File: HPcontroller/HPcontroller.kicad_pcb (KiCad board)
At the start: 4 copper layers, 78 x 57 mm, 65 parts, among them J1 54-00174, J2 USB_C_Receptacle, J3 Conn_01x04_Pin, J4 Conn_01x01_Pin, J5 54-00174, J6 Conn_01x01_Pin, Q2 AON7410, Q3 Q_Dual_NMOS_S1G1S2G2D2D2D1D1, U1 MCP23017_SO, U10 SN74LVC1G14DBV, U11 SN74LVC1G14DBV, U2 MCP3021A1T-E/OT, U3 HEF4043BT, U4 NCP81071B, U6 SN74LV4052ADR, U7 Adafruit_QTPY_ESP32-C3, U8 IP2721, U9 SN74AHC1G08DBVR

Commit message: v3 routing
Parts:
- removed C5, C9: 1uF, Capacitor_SMD:C_0805_2012Metric_Pad1.18x1.45mm_HandSolder
- removed D2: ESDA6V1BC6, Package_TO_SOT_SMD:SOT-23-6
- removed D_HEAT1, D_HOT1, D_POW1, D_RUN1: LED, LED_SMD:LED_0603_1608Metric_Pad1.05x0.95mm_HandSolder
- removed H2: MountingHole, MountingHole:MountingHole_2.7mm_M2.5
- removed J1: 54-00174, HPfootprint:TENSILITY_54-00174
- removed J3: Conn_01x04_Pin, Connector_PinHeader_2.54mm:PinHeader_1x04_P2.54mm_Vertical
- removed J4, J6: Conn_01x01_Pin, HPfootprint:S7051-42R
- removed MOD1: K7803JT-500R3-LB, HPfootprint:MORNSUN_K7803JT-500R3-LB
- removed Q3: Q_Dual_NMOS_S1G1S2G2D2D2D1D1, Package_SO:SOIC-8_3.9x4.9mm_P1.27mm
- removed RTHERM: 10kTHERM, Resistor_SMD:R_0805_2012Metric_Pad1.20x1.40mm_HandSolder
- removed SWDEC2, SWINC3, SWINC4, SWRUN2: SW_SPST, Button_Switch_SMD:SW_SPST_PTS645
- removed U1: MCP23017_SO, Package_SO:SOIC-28W_7.5x17.9mm_P1.27mm
- added C15: 10uF 50V, Capacitor_SMD:C_1206_3216Metric_Pad1.33x1.80mm_HandSolder, F.Cu at (164.6, 138.5)
- added D1: LED, LED_SMD:LED_0603_1608Metric_Pad1.05x0.95mm_HandSolder, F.Cu at (173.4, 137.8)
- added H4: MountingHole, MountingHole:MountingHole_2.7mm_M2.5, F.Cu at (107.8, 122.8)
- added Q1: ~, hotplate_Library:LFPAK56D, F.Cu at (181.0, 134.5)
- added R11: 100, Resistor_SMD:R_0402_1005Metric_Pad0.72x0.64mm_HandSolder, F.Cu at (168.4, 138.0)
- added R14: 10, Resistor_SMD:R_0402_1005Metric_Pad0.72x0.64mm_HandSolder, F.Cu at (172.9, 135.0)
- added R15: 10, Resistor_SMD:R_0402_1005Metric_Pad0.72x0.64mm_HandSolder, F.Cu at (172.9, 136.2)
- added R16: 5k1 1%, Resistor_SMD:R_0402_1005Metric_Pad0.72x0.64mm_HandSolder, F.Cu at (176.0, 126.9)
- added R17: 5k1 1%, Resistor_SMD:R_0402_1005Metric_Pad0.72x0.64mm_HandSolder, F.Cu at (176.0, 129.3)
- added R6: 26k, Resistor_SMD:R_0603_1608Metric_Pad0.98x0.95mm_HandSolder, F.Cu at (175.6, 131.5)
- added RTHERM1: 100kTherm, Resistor_SMD:R_0805_2012Metric_Pad1.20x1.40mm_HandSolder, F.Cu at (135.3, 147.0)
- added TP1: TestPoint, TestPoint:TestPoint_Pad_D1.5mm, F.Cu at (163.2, 127.7)
- added TP2: TestPoint, TestPoint:TestPoint_Pad_D1.5mm, F.Cu at (158.2, 126.5)
- added TP8: TestPoint, TestPoint:TestPoint_Pad_D1.5mm, F.Cu at (171.0, 140.0)
- added TP_3V1: TestPoint, TestPoint:TestPoint_Pad_D1.0mm, F.Cu at (152.8, 143.6)
- added U5: AP33771C, Package_DFN_QFN:DFN-14-1EP_3x3mm_P0.4mm_EP1.78x2.35mm, F.Cu at (172.8, 131.1)
- C14: value 10uF -> 1uF 25V; footprint Capacitor_SMD:C_0805_2012Metric -> Capacitor_SMD:C_0402_1005Metric_Pad0.74x0.62mm_HandSolder
- C6: value 1uF -> 10uF 50V; footprint Capacitor_SMD:C_0603_1608Metric -> Capacitor_SMD:C_1206_3216Metric_Pad1.33x1.80mm_HandSolder
- J2: value USB_C_Receptacle -> UJ20-C-H-G-SMT-1-P16-TR; footprint Connector_USB:USB_C_Receptacle_JAE_DX07S016JA1R1500 -> hotplate_Library:SAMESKY_UJ20-C-H-G-SMT-1-P16-TR
- J5: footprint HPfootprint:TENSILITY_54-00174 -> hotplate_Library:TENSILITY_54-00174
- Q2: value AON7410 -> ~; footprint HPfootprint:DFN3X3A_8L_EPA1_P_AOS -> hotplate_Library:LFPAK56D
- R1: value 5.1k -> 5k1 1%; footprint Resistor_SMD:R_0603_1608Metric -> Resistor_SMD:R_0402_1005Metric_Pad0.72x0.64mm_HandSolder
- R10: value RTHERM -> 100kTherm
- R21: moved to F.Cu
- R4: value 5.1k -> 1k; footprint Resistor_SMD:R_0603_1608Metric -> Resistor_SMD:R_0402_1005Metric_Pad0.72x0.64mm_HandSolder
- R5: value 100k -> 5m; footprint Resistor_SMD:R_0603_1608Metric -> Resistor_SMD:R_0603_1608Metric_Pad0.98x0.95mm_HandSolder
- U3: footprint HPfootprint:SOT109-1_NXP -> Package_SO:SO-16_3.9x9.9mm_P1.27mm
- U7: footprint HPfootprint:QTPY ESP32 C3 -> hotplate_Library:XIAO-ESP32C3-SMD-cutout
- U8: value IP2721 -> ~; footprint Package_SO:TSSOP-16_4.4x5mm_P0.65mm -> hotplate_Library:D78B33-0.5
- moved R21 75.1 mm to (107.9, 139.0)
- moved R22 71.9 mm to (123.4, 143.2), turned to 90 degrees
- moved R24 68.5 mm to (100.8, 133.8), turned to 180 degrees
- moved R13 61.2 mm to (88.5, 128.5), turned to 180 degrees
- moved D_RTD1 61.1 mm to (88.5, 130.5), turned to 180 degrees
- moved C10 59.2 mm to (100.2, 144.7)
- moved SWRST2 57.3 mm to (114.5, 123.7), turned to 90 degrees
- moved R12 55.3 mm to (135.3, 144.7), turned to 180 degrees
- moved C3 55.0 mm to (179.4, 145.7), turned to 0 degrees
- moved U9 54.5 mm to (92.2, 144.8), turned to 180 degrees
- moved R7 53.6 mm to (145.0, 139.2)
- moved R8 53.5 mm to (147.2, 139.2)
- moved H3 53.1 mm to (162.2, 122.8)
- moved R4 52.9 mm to (174.7, 135.5), turned to -90 degrees
- moved C7 52.8 mm to (160.6, 138.0), turned to 90 degrees
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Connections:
- C14 pad 1: +20V_USBPD -> Net-(U5-V5V)
- C2 pad 1: +20V_USBPD -> +28V
- C3 pad 1: +20V_USBPD -> +28V
- C6 pad 1: VBUS -> /USB POWER IN/VUSB_RAW
- C7 pad 1: +20V_USBPD -> +28V
- D3 pad 1: +20V_USBPD -> +28V
- J2 pad A6: unconnected-(J2-D+-PadA6) -> /USB POWER IN/DP
- J2 pad A7: unconnected-(J2-D--PadA7) -> /USB POWER IN/DN
- J2 pad B6: unconnected-(J2-D+-PadB6) -> /USB POWER IN/DP
- J2 pad B7: unconnected-(J2-D--PadB7) -> /USB POWER IN/DN
- Q2 pad 1: +20V_USBPD -> Net-(Q2-S1)
- Q2 pad 2: +20V_USBPD -> Net-(Q2-G1)
- Q2 pad 3: +20V_USBPD -> Net-(Q2-S1)
- Q2 pad 4: Net-(Q2-G) -> Net-(Q2-G2)
- Q2 pad 5: VBUS -> Net-(Q2-D2)
- Q2 pad 7: VBUS -> +28V
- R1 pad 1: /USB POWER IN/CC1 -> /USB POWER IN/CC2
- R4 pad 1: /USB POWER IN/CC2 -> Net-(U5-LED)
- R4 pad 2: GND -> Net-(D1-A)
- R5 pad 1: VBUS -> /USB POWER IN/VUSB_RAW
- R5 pad 2: Net-(U8-SEL) -> Net-(Q2-D2)
- U4 pad 6: +20V_USBPD -> +28V
- U7 pad 10: /INTA -> unconnected-(U7-MISO-Pad10)
- U8 pad 1: Net-(Q2-G) -> +28V
- U8 pad 2: VBUS -> GND
- U8 pad 3: (no net) -> +3V3
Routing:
- net /INTA: track 91.0 -> 0.00 mm, vias 2 -> 0
- net /SDA: track 139.2 -> 60.2 mm
- net GND: track 122.5 -> 53.2 mm, vias 43 -> 32
- net Net-(U4-ENA): track 39.6 -> 101.2 mm, vias 2 -> 0
- net /SCL: track 128.0 -> 68.0 mm, vias 3 -> 2
- net +20V_USBPD: track 55.2 -> 0.00 mm, vias 2 -> 0
- net +28V: track 0.00 -> 48.3 mm
- net /HEATER DRIVE/ENABLE_HEATER_DRIVE: track 74.8 -> 26.7 mm
- net Net-(U3-1S): track 42.2 -> 2.25 mm
- net /Controlpad/RUN_LED: track 29.3 -> 0.00 mm
- net Net-(U2-Ain): track 41.5 -> 12.9 mm
- net /Controlpad/HOT: track 28.4 -> 0.00 mm
- net /Controlpad/POW: track 28.1 -> 0.00 mm
- net /USB POWER IN/VUSB_RAW: track 0.00 -> 26.7 mm, vias 0 -> 2
- net /Controlpad/RUN: track 23.8 -> 0.00 mm
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- added copper zone on F.Cu, net +28V
- added copper zone on In1.Cu, net +3V3
- added copper zone on In2.Cu, net GND
- removed copper zone on F.Cu, net +20V_USBPD
- removed copper zone on In2.Cu, net +3V3
- removed copper zone on In1.Cu, net GND
- removed copper zone on F.Cu, net Net-(D3-A)
- removed copper zone on F.Cu, net VBUS
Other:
- board size 78 x 57 mm -> 100 x 30 mm
- board text removed: "HP_POWER"

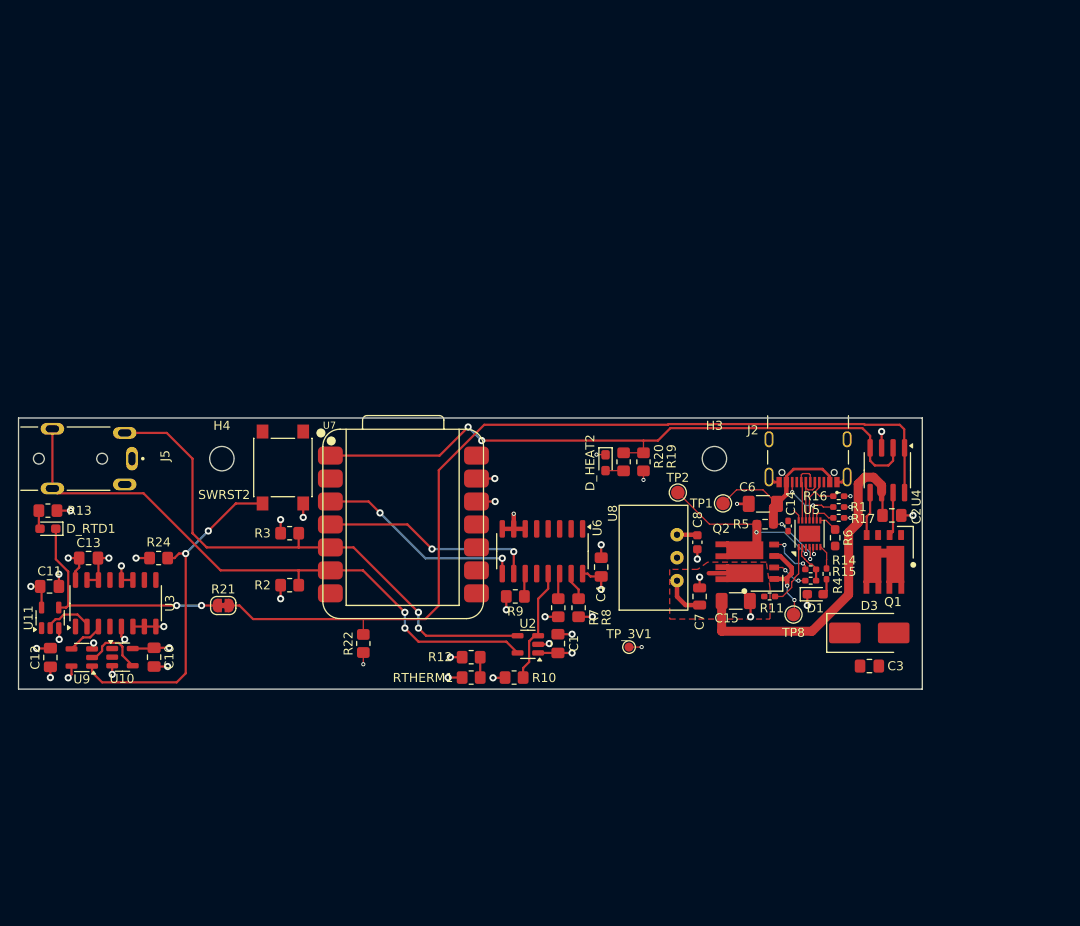
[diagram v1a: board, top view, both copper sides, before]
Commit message: new temp circuit
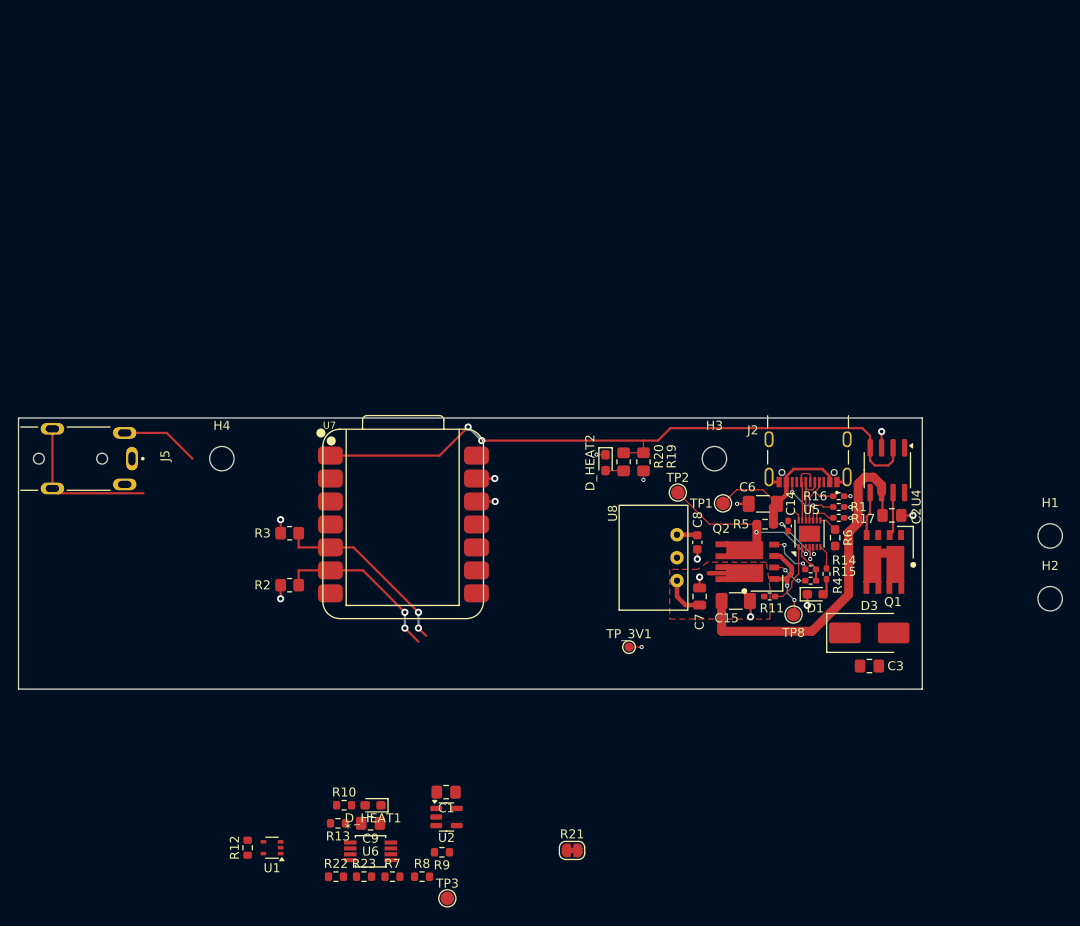
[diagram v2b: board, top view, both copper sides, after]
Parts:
- removed C10, C11, C12, C13, C4: 1uF, Capacitor_SMD:C_0805_2012Metric_Pad1.18x1.45mm_HandSolder
- removed D_RTD1: LED, LED_SMD:LED_0603_1608Metric_Pad1.05x0.95mm_HandSolder
- removed R24: 10k, Resistor_SMD:R_0805_2012Metric_Pad1.20x1.40mm_HandSolder
- removed RTHERM1: 100kTherm, Resistor_SMD:R_0805_2012Metric_Pad1.20x1.40mm_HandSolder
- removed SWRST2: SW_SPST, Button_Switch_SMD:SW_SPST_PTS645
- removed U10, U11: SN74LVC1G14DBV, Package_TO_SOT_SMD:SOT-23-5
- removed U3: HEF4043BT, Package_SO:SO-16_3.9x9.9mm_P1.27mm
- removed U9: SN74AHC1G08DBVR, Package_TO_SOT_SMD:SOT-23-5
- added C9: 1uF, Capacitor_SMD:C_0805_2012Metric_Pad1.18x1.45mm_HandSolder, F.Cu at (124.2, 163.1)
- added D_HEAT1: LED, LED_SMD:LED_0603_1608Metric_Pad1.05x0.95mm_HandSolder, F.Cu at (124.5, 161.1)
- added H1: MountingHole, MountingHole:MountingHole_2.7mm_M2.5, F.Cu at (199.4, 131.3)
- added H2: MountingHole, MountingHole:MountingHole_2.7mm_M2.5, F.Cu at (199.4, 138.2)
- added R23: 952, Resistor_SMD:R_0603_1608Metric, F.Cu at (123.5, 169.0)
- added TP3: TestPoint, TestPoint:TestPoint_Pad_D1.5mm, F.Cu at (132.7, 171.4)
- added U1: PSSI2021SAY, Package_TO_SOT_SMD:SOT-353_SC-70-5, F.Cu at (113.3, 165.8)
- R10: value 100kTherm -> 100; footprint Resistor_SMD:R_0805_2012Metric_Pad1.20x1.40mm_HandSolder -> Resistor_SMD:R_0603_1608Metric
- R12: value 420 -> 626; footprint Resistor_SMD:R_0805_2012Metric_Pad1.20x1.40mm_HandSolder -> Resistor_SMD:R_0603_1608Metric
- R13: value 100 -> 2k; footprint Resistor_SMD:R_0805_2012Metric_Pad1.20x1.40mm_HandSolder -> Resistor_SMD:R_0603_1608Metric
- R22: value 10k -> 1666; footprint Resistor_SMD:R_0805_2012Metric_Pad1.20x1.40mm_HandSolder -> Resistor_SMD:R_0603_1608Metric
- R7: value 100k -> 111; footprint Resistor_SMD:R_0805_2012Metric_Pad1.20x1.40mm_HandSolder -> Resistor_SMD:R_0603_1608Metric
- R8: value 10k -> 1000; footprint Resistor_SMD:R_0805_2012Metric_Pad1.20x1.40mm_HandSolder -> Resistor_SMD:R_0603_1608Metric
- R9: value 1k -> 0; footprint Resistor_SMD:R_0805_2012Metric_Pad1.20x1.40mm_HandSolder -> Resistor_SMD:R_0603_1608Metric
- U6: value SN74LV4052ADR -> LM2904; footprint Package_SO:SOIC-16_3.9x9.9mm_P1.27mm -> hotplate_Library:MINISO8_3P1X3P2X0P65_STM
- moved R13 47.2 mm to (120.6, 163.1)
- moved R21 47.2 mm to (146.5, 166.1)
- moved U6 38.3 mm to (124.2, 166.2), turned to 0 degrees
- moved R7 35.0 mm to (126.6, 169.0), turned to 0 degrees
- moved R8 34.4 mm to (129.9, 169.0), turned to 0 degrees
- moved R12 32.5 mm to (110.6, 165.8), turned to 90 degrees
- moved R9 29.4 mm to (132.1, 166.3)
- moved R22 26.0 mm to (120.4, 169.0), turned to 0 degrees
- moved R10 23.5 mm to (121.3, 161.1)
- moved U2 21.1 mm to (132.6, 162.4), turned to 0 degrees
- moved C1 20.6 mm to (132.6, 159.7), turned to 0 degrees
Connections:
- R10 pad 2: Net-(U2-Ain) -> Net-(D_HEAT1-A)
- R12 pad 1: Net-(U3-1S) -> +3V3
- R12 pad 2: GND -> Net-(R12-Pad2)
- R13 pad 1: +3V3 -> Net-(U2-Ain)
- R13 pad 2: Net-(D_RTD1-A) -> Net-(U6A--)
- R22 pad 2: Net-(U4-ENA) -> Net-(U6A--)
- R7 pad 1: Net-(U6-1Y1) -> Net-(U6B-+)
- R7 pad 2: GND -> Net-(D4-A)
- R8 pad 1: Net-(U6-1Y2) -> Net-(D4-A)
- R9 pad 1: Net-(U6-1Y3) -> Net-(D4-K)
- R9 pad 2: GND -> Net-(R9-Pad2)
- U6 pad 1: unconnected-(U6-2Y0-Pad1) -> Net-(U2-Ain)
- U6 pad 2: unconnected-(U6-2Y2-Pad2) -> Net-(U6A--)
- U6 pad 3: unconnected-(U6-2-COM-Pad3) -> Net-(U6A-+)
- U6 pad 4: unconnected-(U6-2Y3-Pad4) -> GND
- U6 pad 5: unconnected-(U6-2Y1-Pad5) -> Net-(U6B-+)
- U6 pad 6: GND -> Net-(U2-Ain)
- U6 pad 7: GND -> /HEATER DRIVE/ENABLE_HEATER_DRIVE
- U6 pad 8: GND -> +3V3
- U7 pad 3: /SEL_B -> unconnected-(U7-A2-Pad3)
- U7 pad 4: /SEL_A -> unconnected-(U7-A3-Pad4)
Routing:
- net Net-(U4-ENA): track 101.2 -> 0.00 mm
- net Net-(SWRST2-A): track 38.4 -> 0.00 mm, vias 2 -> 0
- net GND: track 53.2 -> 18.7 mm, vias 32 -> 14
- net /SCL: track 68.0 -> 35.8 mm
- net /SDA: track 60.2 -> 29.4 mm
- net +3V3: track 38.9 -> 8.74 mm, vias 17 -> 4
- net /HEATER DRIVE/ENABLE_HEATER_DRIVE: track 26.7 -> 0.00 mm, vias 2 -> 0
- net /SEL_A: track 24.0 -> 0.00 mm, vias 2 -> 0
- net /SEL_B: track 23.3 -> 0.00 mm, vias 2 -> 0
- net Net-(U2-Ain): track 12.9 -> 0.00 mm
- net Net-(U10-Pad4): track 7.07 -> 0.00 mm
- net /ThermalProtector/QOUT: track 5.64 -> 0.00 mm
- net Net-(U3-1R): track 4.17 -> 0.00 mm
- net Net-(U6-1Y2): track 3.12 -> 0.00 mm
- net Net-(U6-1Y1): track 2.84 -> 0.00 mm
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
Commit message: finished temp meas stuff, laying out
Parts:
- added C4: 1uF, Capacitor_SMD:C_0805_2012Metric, F.Cu at (147.0, 145.6)
- added D2: BAR43FILM, Package_TO_SOT_SMD:SOT-23, F.Cu at (139.5, 131.5)
- added R18: RTD PT1000, Resistor_SMD:R_0805_2012Metric, F.Cu at (137.5, 146.0)
- added SW1: SW_SPST, hotplate_Library:SW_EVQ-P7J01P, F.Cu at (137.5, 120.0)
- added TP4: TestPoint, TestPoint:TestPoint_Pad_D1.5mm, F.Cu at (134.0, 146.5)
- added TP5: TestPoint, TestPoint:TestPoint_Pad_D1.5mm, F.Cu at (131.5, 138.5)
- added TP6: TestPoint, TestPoint:TestPoint_Pad_D1.5mm, F.Cu at (137.0, 143.0)
- added TP7: TestPoint, TestPoint:TestPoint_Pad_D1.5mm, F.Cu at (142.0, 138.5)
- added TP9: TestPoint, TestPoint:TestPoint_Pad_D1.5mm, F.Cu at (137.0, 127.0)
- C1, C2, C3, C9: footprint Capacitor_SMD:C_0805_2012Metric_Pad1.18x1.45mm_HandSolder -> Capacitor_SMD:C_0805_2012Metric
- C14: footprint Capacitor_SMD:C_0402_1005Metric_Pad0.74x0.62mm_HandSolder -> Capacitor_SMD:C_0402_1005Metric
- R1, R11, R14, R15, R16, R17, R4: footprint Resistor_SMD:R_0402_1005Metric_Pad0.72x0.64mm_HandSolder -> Resistor_SMD:R_0402_1005Metric
- R13: value 2k -> 1210
- R22: value 1666 -> 1300
- R23: value 952 -> 1020
- R5, R6: footprint Resistor_SMD:R_0603_1608Metric_Pad0.98x0.95mm_HandSolder -> Resistor_SMD:R_0603_1608Metric
- R7: value 111 -> 120
- R8: value 1000 -> 1200
- TP_3V1: footprint TestPoint:TestPoint_Pad_D1.0mm -> TestPoint:TestPoint_Pad_D1.5mm
- moved TP3 41.6 mm to (169.0, 151.0)
- moved R12 40.0 mm to (145.0, 145.3), turned to -90 degrees
- moved R21 39.9 mm to (133.2, 128.5)
- moved R7 38.7 mm to (142.0, 133.5), turned to 180 degrees
- moved R8 36.1 mm to (142.0, 135.0)
- moved U1 35.5 mm to (142.3, 145.3), turned to 0 degrees
- moved R9 34.6 mm to (136.5, 132.0), turned to -90 degrees
- moved U6 32.1 mm to (137.5, 137.0), turned to 90 degrees
- moved D_HEAT1 31.3 mm to (132.9, 131.0)
- moved R22 29.8 mm to (134.0, 142.5)
- moved R10 29.6 mm to (132.0, 133.5), turned to 90 degrees
- moved C9 29.3 mm to (134.0, 135.5), turned to -90 degrees
- moved R23 27.1 mm to (134.0, 144.0), turned to 180 degrees
- moved R13 25.8 mm to (134.0, 141.0), turned to 0 degrees
- moved U2 20.6 mm to (129.5, 142.0), turned to 180 degrees
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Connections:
- R7 pad 1: Net-(U6B-+) -> +3V3
- R7 pad 2: Net-(D4-A) -> Net-(D2-A)
- R8 pad 1: Net-(D4-A) -> Net-(D2-A)
- R9 pad 2: Net-(R9-Pad2) -> /HEATER DRIVE/ENABLE_HEATER_DRIVE
- U6 pad 5: Net-(U6B-+) -> Net-(D2-A)
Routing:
- net Net-(U4-ENA): track 0.00 -> 58.3 mm
- net Net-(SW1-B): track 0.00 -> 36.3 mm, vias 0 -> 2
- net +3V3: track 8.74 -> 26.3 mm, vias 4 -> 11
- net /SCL: track 35.8 -> 53.3 mm, vias 2 -> 0
- net /HEATER DRIVE/ENABLE_HEATER_DRIVE: track 0.00 -> 14.9 mm
- net GND: track 18.7 -> 33.2 mm, vias 14 -> 22
- net Net-(U6A-+): track 0.00 -> 14.3 mm
- net /SDA: track 29.4 -> 42.8 mm, vias 2 -> 0
- net Net-(D2-A): track 0.00 -> 11.4 mm
- net /HEAT_DRIVE: track 73.2 -> 83.2 mm, vias 2 -> 0
- net Net-(U6A--): track 0.00 -> 9.30 mm
- net Net-(D2-K): track 0.00 -> 3.52 mm
- net Net-(R12-Pad2): track 0.00 -> 1.82 mm
- net Net-(D_HEAT1-A): track 0.00 -> 1.68 mm

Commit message: routing
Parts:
- added J1: Conn_01x02_Pin, hpfootprint:S7051-42R_array, F.Cu at (139.2, 156.0)
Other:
- board size 100 x 30 mm -> 100 x 39.8 mm
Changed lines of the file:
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@@
 		)
 	)
+	(footprint "hpfootprint:S7051-42R_array"
+		(layer "F.Cu")
+		(at 139.25 156)
+		(property "Reference" "J1"
+			(at -0.2 -2.1 0)
+			(unlocked yes)
+			(layer "F.SilkS")
+			(effects
+				(font
+					(size 1 1)
+					(thickness 0.15)
+				)
+			)
+		)
+		(property "Value" "Conn_01x02_Pin"
+			(at 0 1 0)
+			(unlocked yes)
+			(layer "F.Fab")
+			(effects
+				(font
+					(size 1 1)
+					(thickness 0.15)
+				)
+			)
+		)
+		(property "Datasheet" "~"
+			(at 0 0 0)
+			(layer "F.Fab")
+			(hide yes)
+			(effects
+				(font
+					(size 1.27 1.27)
+					(thickness 0.15)
+				)
+			)
+		)
+		(property "Description" "Generic connector, single row, 01x02, script generated"
+			(at 0 0 0)
+			(layer "F.Fab")
+			(hide yes)
+			(effects
+				(font
+					(size 1.27 1.27)
+					(thickness 0.15)
+				)
+			)
+		)
+		(property ki_fp_filters "Connector*:*_1x??_*")
+		(sheetname "/HEATER DRIVE/")
+		(sheetfile "HeaterDrive.kicad_sch")
+		(attr smd)
+		(fp_text user "${REFERENCE}"
+			(at 0 2.5 0)
+			(unlocked yes)
+			(layer "F.Fab")
+			(effects
+				(font
+					(size 1 1)
+					(thickness 0.15)
+				)
+			)
+		)
+		(pad "1" smd roundrect
+			(at 4 0)
+			(size 4.5 2.9)
+			(layers "F.Cu" "F.Mask" "F.Paste")
+			(roundrect_rratio 0.08620689655)
+			(net 7 "+28V")
+			(pinfunction "Pin_1")
+			(pintype "passive")
+			(thermal_bridge_angle 45)
+		)
+		(pad "1" smd roundrect
+			(at 9.25 0)
+			(size 4.5 2.9)
+			(layers "F.Cu" "F.Mask" "F.Paste")
+			(roundrect_rratio 0.08620689655)
+			(net 7 "+28V")
+			(pinfunction "Pin_1")
+			(pintype "passive")
+			(thermal_bridge_angle 45)
+		)
+		(pad "1" smd roundrect
+			(at 14.5 0)
+			(size 4.5 2.9)
+			(layers "F.Cu" "F.Mask" "F.Paste")
+			(roundrect_rratio 0.08620689655)
+			(net 7 "+28V")
+			(pinfunction "Pin_1")
+			(pintype "passive")
+			(thermal_bridge_angle 45)
+		)
+		(pad "2" smd roundrect
+			(at -14.5 0)
+			(size 4.5 2.9)
+			(layers "F.Cu" "F.Mask" "F.Paste")
+			(roundrect_rratio 0.08620689655)
+			(net 9 "Net-(D3-A)")
+			(pinfunction "Pin_2")
+			(pintype "passive")
+			(thermal_bridge_angle 45)
+		)
+		(pad "2" smd roundrect
+			(at -9.25 0)
+			(size 4.5 2.9)
+			(layers "F.Cu" "F.Mask" "F.Paste")
+			(roundrect_rratio 0.08620689655)
+			(net 9 "Net-(D3-A)")
+			(pinfunction "Pin_2")
+			(pintype "passive")
+			(thermal_bridge_angle 45)
+		)
+		(pad "2" smd roundrect
+			(at -4 0)
+			(size 4.5 2.9)
+			(layers "F.Cu" "F.Mask" "F.Paste")
+			(roundrect_rratio 0.08620689655)
+			(net 9 "Net-(D3-A)")
+			(pinfunction "Pin_2")
+			(pintype "passive")
+			(thermal_bridge_angle 45)
+		)
+		(embedded_fonts no)
+	)
 	(footprint "MountingHole:MountingHole_2.7mm_M2.5"
 		(layer "F.Cu")
@@
 	(gr_rect
 		(start 85.25 118.25)
-		(end 185.25 148.25)
+		(end 185.25 158)
 		(stroke
 			(width 0.1)

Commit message: uploading routing
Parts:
- removed TP3: TestPoint, TestPoint:TestPoint_Pad_D1.5mm
- moved H1 75.8 mm to (126.2, 151.2)
- moved H2 56.7 mm to (144.2, 151.2)
- moved C3 9.60 mm to (170.0, 143.8), turned to 180 degrees
- moved J1 4.00 mm to (135.2, 156.0), turned to 180 degrees
- moved C4 3.71 mm to (146.8, 141.8)
- moved R12 3.71 mm to (144.8, 141.7)
- moved U1 3.71 mm to (142.1, 141.7)
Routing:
- net +28V: track 48.3 -> 117.6 mm
- net Net-(D3-A): track 2.54 -> 66.9 mm
- net GND: track 33.2 -> 42.6 mm, vias 22 -> 29
- net Net-(U6A-+): track 14.3 -> 13.3 mm
